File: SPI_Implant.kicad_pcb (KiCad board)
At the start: 2 copper layers, 32 x 20 mm, 6 parts, among them J1 Dediprog_FPC, J2 SPI_Socket, U3 TMUX1511PWR, U4 TMUX1511PWR

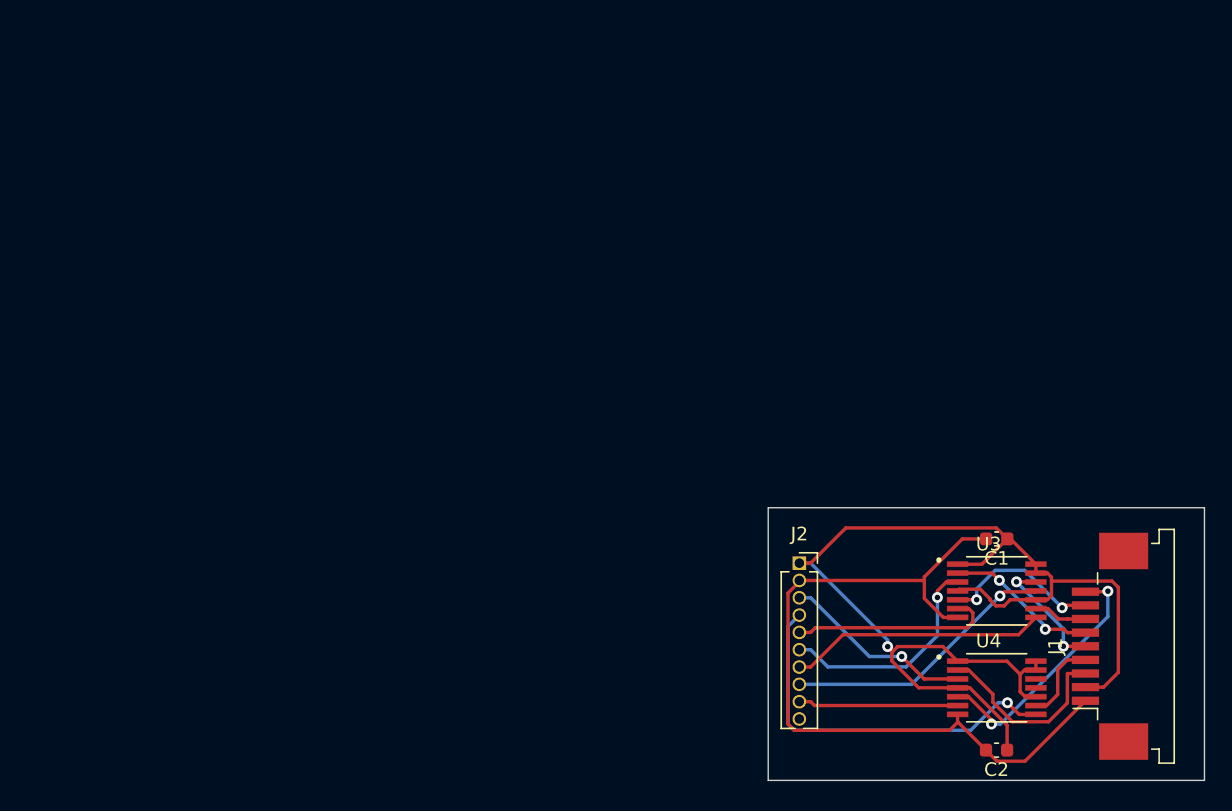
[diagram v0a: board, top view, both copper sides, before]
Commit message: updated footprints and routing, added labels
Signed-off-by: Andy Ebrahiem <andy@9elements.com>
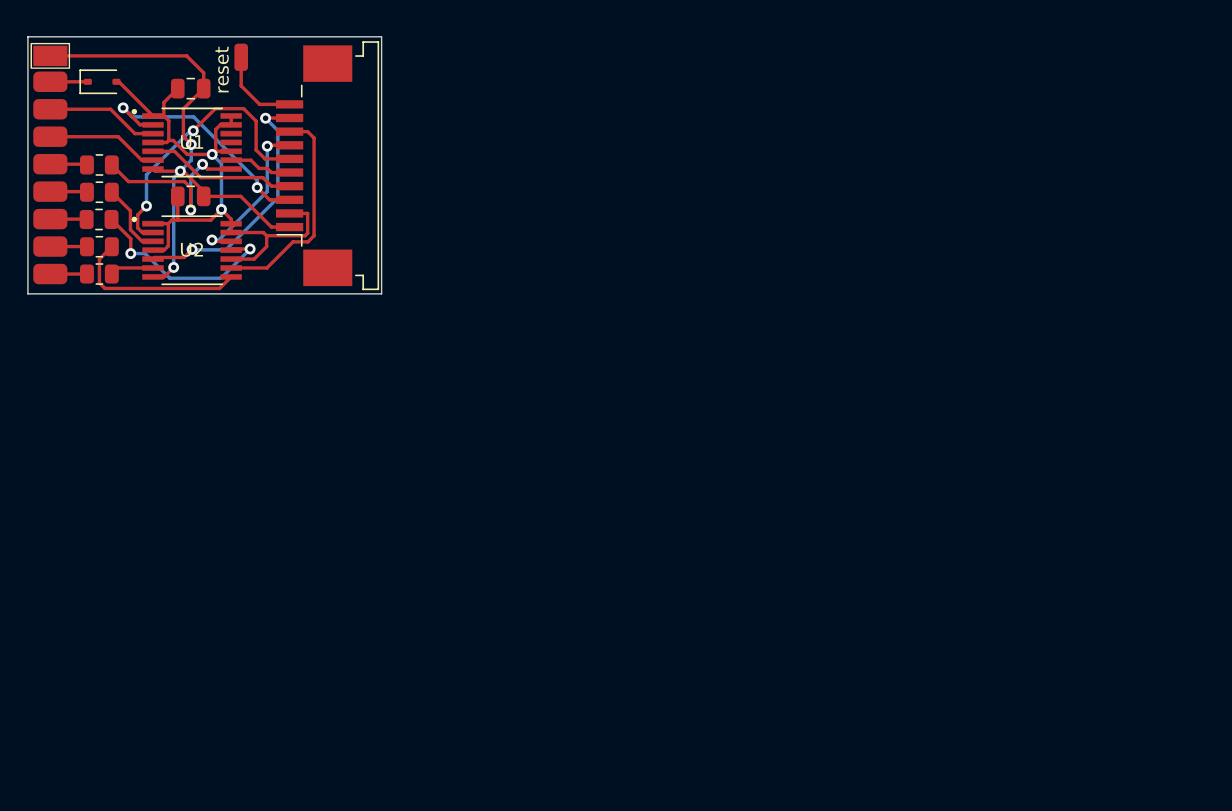
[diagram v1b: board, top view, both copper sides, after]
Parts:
- added D1: BAT60A, Diode_SMD:D_SOD-323, F.Cu at (5.50, 3.30)
- added G***: LOGO, pi_hat_spi_v2:9elogo, B.Cu at (21.0, 14.9)
- added J3: Conn_01x01, Connector_Wire:SolderWirePad_1x01_SMD_1x2mm, F.Cu at (15.7, 1.50)
- added R1: 100, Resistor_SMD:R_0805_2012Metric, F.Cu at (5.30, 9.40)
- added R2: 100, Resistor_SMD:R_0805_2012Metric, F.Cu at (5.30, 17.4)
- added R3: 100, Resistor_SMD:R_0805_2012Metric, F.Cu at (5.30, 15.4)
- added R4: 100, Resistor_SMD:R_0805_2012Metric, F.Cu at (5.28, 13.4)
- added R5: 100, Resistor_SMD:R_0805_2012Metric, F.Cu at (5.30, 11.4)
- C1, C2: footprint Capacitor_SMD:C_0603_1608Metric -> Capacitor_SMD:C_0805_2012Metric
- J1: value Dediprog_FPC -> Conn_01x10_Socket; footprint Connector_FFC-FPC:TE_84952-9_1x09-1MP_P1.0mm_Horizontal -> Connector_FFC-FPC:TE_1-84952-0_1x10-1MP_P1.0mm_Horizontal
- J2: footprint Connector_PinSocket_1.27mm:PinSocket_1x10_P1.27mm_Vertical -> pad:wire_pad_row_1x09-2x3mm
- moved C2 76.5 mm to (12.0, 3.80), turned to 0 degrees
- moved U1 71.3 mm to (12.1, 7.75)
- moved J1 68.2 mm to (21.1, 9.46)
- moved J2 66.4 mm to (1.70, 1.40), turned to -90 degrees
- moved C1 64.2 mm to (12.0, 11.7), turned to 0 degrees
- moved U2 64.1 mm to (12.1, 15.7)
- renumbered U4 to U1, U3 to U2
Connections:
- J1 pad 4: P_CLK -> P_CS2
- J1 pad 5: P_MISO -> P_CLK
- J1 pad 7: P_IO2 -> P_MISO
- J1 pad 8: P_IO3 -> P_IO2
- J1 pad 9: P_CS2 -> P_IO3
- J2 pad 1: +3.3V -> GND
- J2 pad 2: GND -> Net-(D1-K)
- J2 pad 4: CLK -> CS2
- J2 pad 5: MISO -> Net-(J2-Pin_5)
- J2 pad 6: MOSI -> Net-(J2-Pin_6)
- J2 pad 7: IO2 -> Net-(J2-Pin_7)
- J2 pad 8: IO3 -> Net-(J2-Pin_8)
- J2 pad 9: CS2 -> Net-(J2-Pin_9)
- U2 pad 11: IO3 -> MISO
- U2 pad 6: MISO -> IO3
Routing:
- net +3.3V: track 86.8 -> 47.5 mm, vias 1 -> 2
- net IO3: track 20.2 -> 3.20 mm, vias 1 -> 0
- net GND: track 56.3 -> 41.2 mm, vias 0 -> 3
- net CLK: track 27.9 -> 14.1 mm, vias 1 -> 2
- net P_IO2: track 3.96 -> 16.2 mm
- net MOSI: track 16.6 -> 5.32 mm, vias 1 -> 0
- net P_MOSI: track 11.3 -> 20.7 mm
- net P_CS2: track 18.8 -> 11.1 mm, vias 2 -> 0
- net P_IO3: track 11.9 -> 19.0 mm
- net Net-(J1-Pin_10): track 0.00 -> 6.21 mm
- net CS1: track 14.1 -> 8.27 mm, vias 1 -> 0
- net IO2: track 18.9 -> 13.2 mm
- net P_CS1: track 14.0 -> 18.0 mm, vias 0 -> 2
- net CS2: track 11.7 -> 8.24 mm
- net P_MISO: track 9.20 -> 12.0 mm
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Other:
- board size 32 x 20 mm -> 25.9 x 18.9 mm
- board text added: "CLK"
- board text added: "CS1"
- board text added: "CS2"
- board text added: "GND"
- board text added: "IO2"
- board text added: "IO3"
- board text added: "MISO"
- board text added: "MOSI"
- board text added: "VCC"
- board text added: "reset"
